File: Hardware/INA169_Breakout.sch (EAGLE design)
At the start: 21 parts, among them U1 INA169

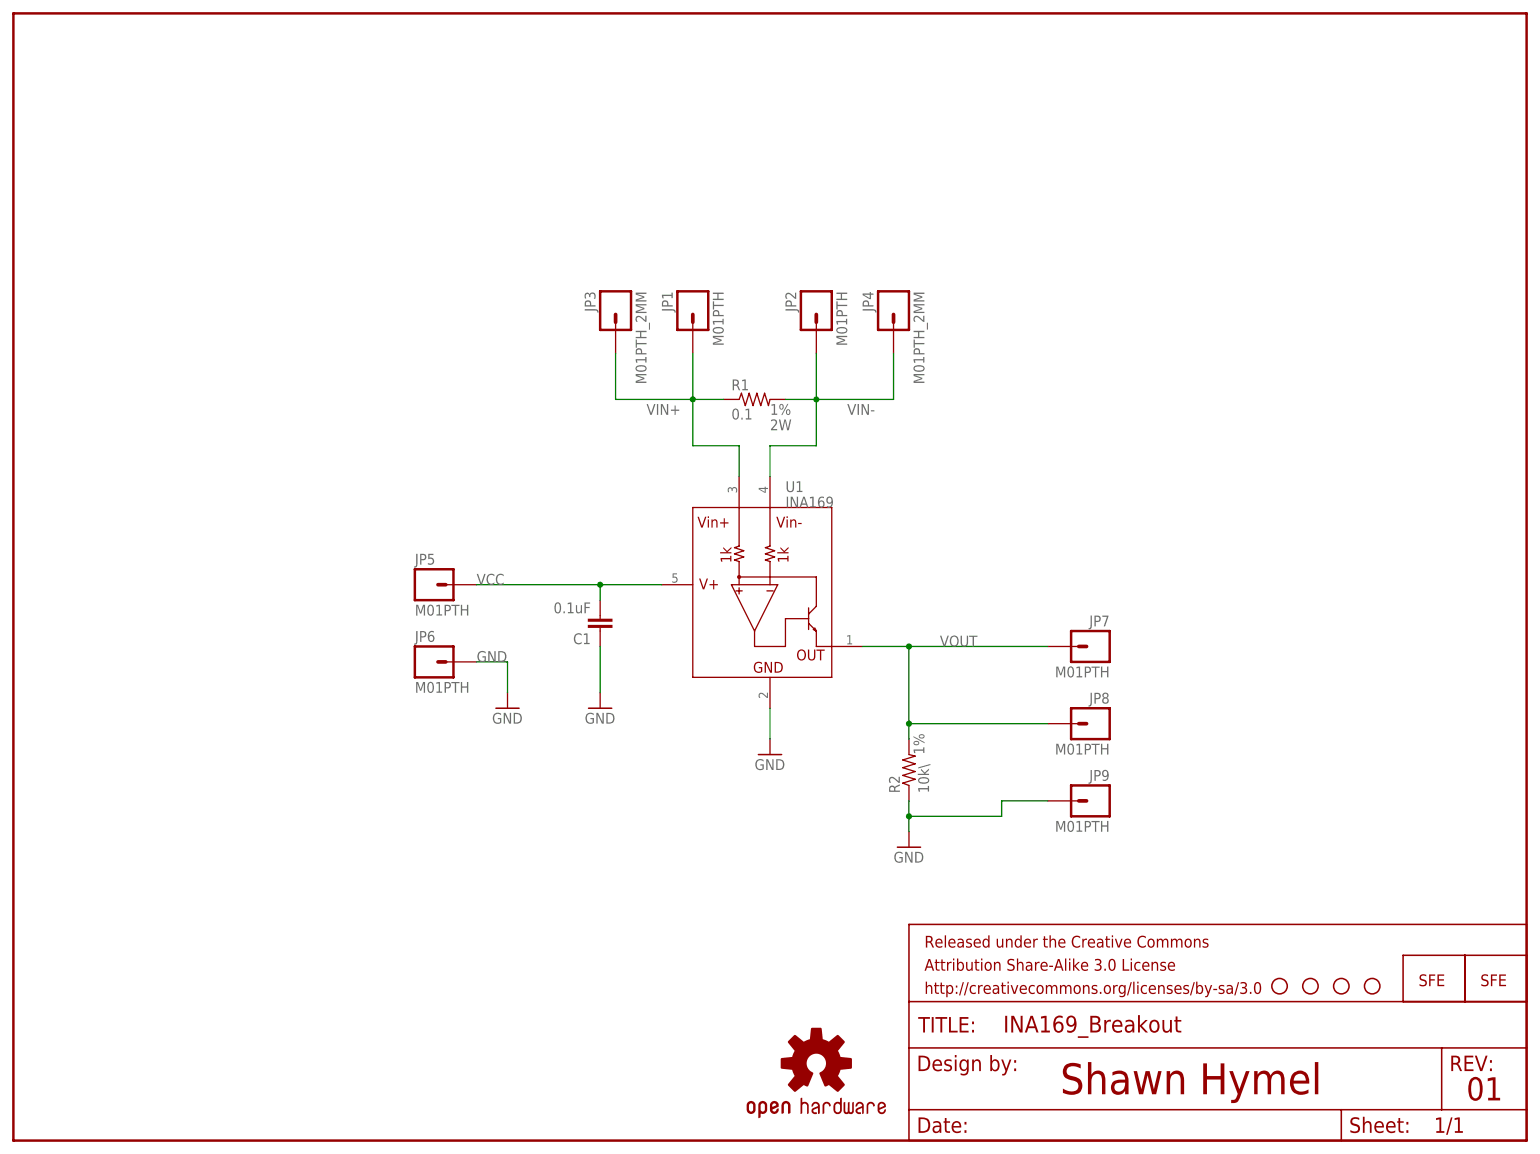
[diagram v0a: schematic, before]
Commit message: Fixed changes from board review. Ready for prototype.
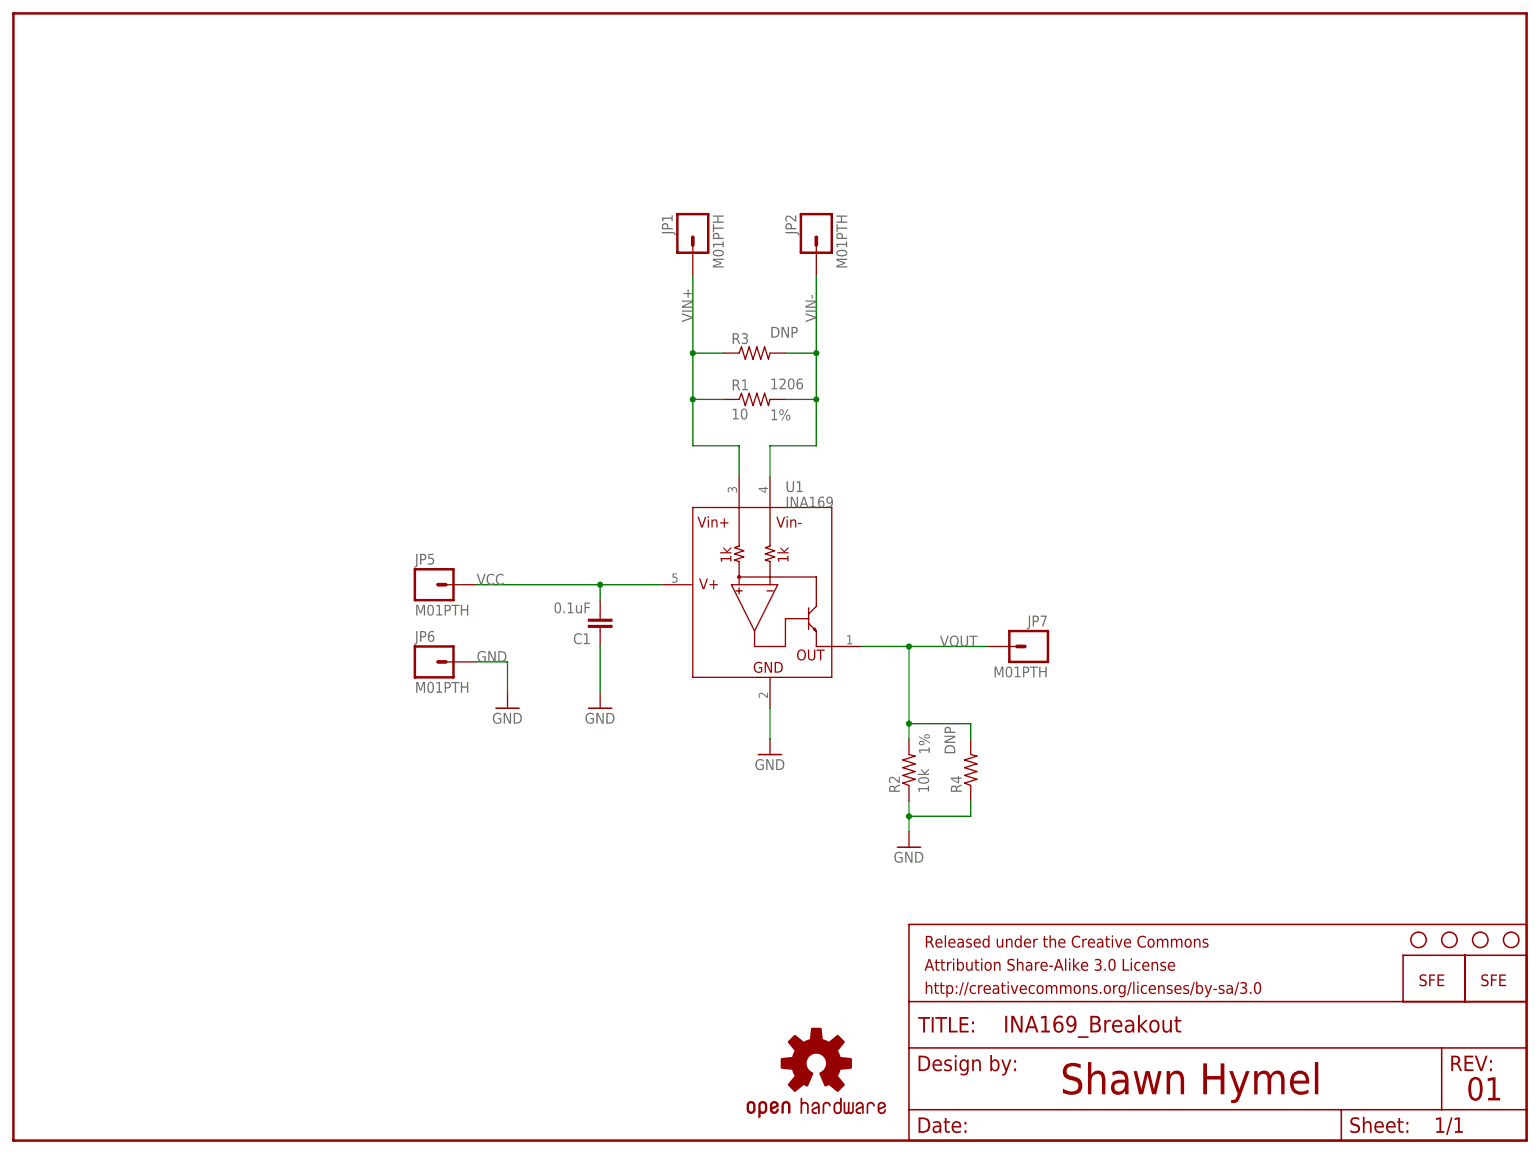
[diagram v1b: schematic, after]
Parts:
- removed JP3, JP4: M01PTH_2MM, SparkFun-Connectors:M01PTH_2MM
- removed JP8, JP9: M01PTH, SparkFun-Connectors:M01PTH
- added R3: (no value), SparkFun-Resistors:RESISTORPTH-2W
- added R4: (no value), SparkFun-Resistors:RESISTORPTH-1/4W
- R1: value 0.1 -> 10; device SparkFun-Passives:RESISTOR2512 -> SparkFun-Resistors:RESISTOR1206; POW 2W -> (none); SIZE (none) -> 1206
- R2: value 10k\ -> 10k; device SparkFun-Passives:RESISTOR0603-RES -> SparkFun-Resistors:RESISTOR0603
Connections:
- net GND: now also R4.1; no longer JP9.1
- net VIN+: now also R3.1; no longer JP3.1
- net VIN-: now also R3.2; no longer JP4.1
- net VOUT: now also R4.2; no longer JP8.1
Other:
- moved on the sheet: JP1, JP2, JP7
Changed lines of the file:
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@@
 <drawing>
 <settings>
-<setting alwaysvectorfont="no"/>
+<setting alwaysvectorfont="yes"/>
 <setting verticaltext="up"/>
 </settings>
@@
 <part name="FRAME1" library="SparkFun-Aesthetics" deviceset="FRAME-LETTER" device=""/>
 <part name="U1" library="SparkFun-AnalogIC" deviceset="INA169" device=""/>
-<part name="R1" library="SparkFun-Passives" deviceset="RESISTOR" device="2512" value="0.1">
-<attribute name="POW" value="2W"/>
-<attribute name="TOL" value="1%"/>
-</part>
 <part name="JP1" library="SparkFun-Connectors" deviceset="M01" device="PTH"/>
 <part name="JP2" library="SparkFun-Connectors" deviceset="M01" device="PTH"/>
-<part name="JP3" library="SparkFun-Connectors" deviceset="M01" device="PTH_2MM"/>
-<part name="JP4" library="SparkFun-Connectors" deviceset="M01" device="PTH_2MM"/>
 <part name="JP5" library="SparkFun-Connectors" deviceset="M01" device="PTH"/>
 <part name="JP6" library="SparkFun-Connectors" deviceset="M01" device="PTH"/>
 <part name="JP7" library="SparkFun-Connectors" deviceset="M01" device="PTH"/>
-<part name="R2" library="SparkFun-Passives" deviceset="RESISTOR" device="0603-RES" value="10k\">
-<attribute name="TOL" value="1%"/>
-</part>
 <part name="C1" library="SparkFun-Passives" deviceset="CAP" device="0603-CAP" value="0.1uF"/>
 <part name="STANDOFF1" library="SparkFun-Electromechanical" deviceset="STAND-OFF" device=""/>
@@
 <part name="GND3" library="SparkFun-Aesthetics" deviceset="GND" device=""/>
 <part name="GND4" library="SparkFun-Aesthetics" deviceset="GND" device=""/>
-<part name="JP8" library="SparkFun-Connectors" deviceset="M01" device="PTH"/>
-<part name="JP9" library="SparkFun-Connectors" deviceset="M01" device="PTH"/>
+<part name="R3" library="SparkFun-Resistors" deviceset="RESISTOR" device="PTH-2W">
+<attribute name="PLACE" value="DNP"/>
+</part>
+<part name="R4" library="SparkFun-Resistors" deviceset="RESISTOR" device="PTH-1/4W">
+<attribute name="PLACE" value="DNP"/>
+</part>
+<part name="R2" library="SparkFun-Resistors" deviceset="RESISTOR" device="0603" value="10k">
+<attribute name="TOL" value="1%"/>
+</part>
+<part name="R1" library="SparkFun-Resistors" deviceset="RESISTOR" device="1206" value="10">
+<attribute name="SIZE" value="1206"/>
+<attribute name="TOL" value="1%"/>
+</part>
 </parts>
 <sheets>
@@
 <instance part="FRAME1" gate="G$2" x="147.32" y="0"/>
 <instance part="U1" gate="G$1" x="124.46" y="88.9"/>
-<instance part="R1" gate="G$1" x="121.92" y="121.92">
-<attribute name="TOL" x="124.46" y="119.38" size="1.778" layer="96"/>
-<attribute name="POW" x="124.46" y="116.84" size="1.778" layer="96"/>
-</instance>
-<instance part="JP1" gate="G$1" x="111.76" y="137.16" rot="MR270"/>
-<instance part="JP2" gate="G$1" x="132.08" y="137.16" rot="MR270"/>
-<instance part="JP3" gate="G$1" x="99.06" y="137.16" rot="MR270"/>
-<instance part="JP4" gate="G$1" x="144.78" y="137.16" rot="MR270"/>
+<instance part="JP1" gate="G$1" x="111.76" y="149.86" rot="MR270"/>
+<instance part="JP2" gate="G$1" x="132.08" y="149.86" rot="MR270"/>
 <instance part="JP5" gate="G$1" x="68.58" y="91.44"/>
 <instance part="JP6" gate="G$1" x="68.58" y="78.74"/>
-<instance part="JP7" gate="G$1" x="177.8" y="81.28" rot="MR0"/>
-<instance part="R2" gate="G$1" x="147.32" y="60.96" rot="R90">
-<attribute name="TOL" x="149.86" y="63.5" size="1.778" layer="96" rot="R90"/>
-</instance>
+<instance part="JP7" gate="G$1" x="167.64" y="81.28" rot="MR0"/>
 <instance part="C1" gate="G$1" x="96.52" y="86.36" rot="R180"/>
-<instance part="STANDOFF1" gate="G$1" x="223.52" y="25.4"/>
-<instance part="STANDOFF2" gate="G$1" x="218.44" y="25.4"/>
-<instance part="STANDOFF3" gate="G$1" x="213.36" y="25.4"/>
-<instance part="STANDOFF4" gate="G$1" x="208.28" y="25.4"/>
+<instance part="STANDOFF1" gate="G$1" x="246.38" y="33.02"/>
+<instance part="STANDOFF2" gate="G$1" x="241.3" y="33.02"/>
+<instance part="STANDOFF3" gate="G$1" x="236.22" y="33.02"/>
+<instance part="STANDOFF4" gate="G$1" x="231.14" y="33.02"/>
 <instance part="LOGO1" gate="G$1" x="241.3" y="25.4"/>
 <instance part="LOGO2" gate="G$1" x="132.08" y="12.7"/>
@@
 <instance part="GND3" gate="1" x="124.46" y="63.5"/>
 <instance part="GND4" gate="1" x="147.32" y="48.26"/>
-<instance part="JP8" gate="G$1" x="177.8" y="68.58" rot="MR0"/>
-<instance part="JP9" gate="G$1" x="177.8" y="55.88" rot="MR0"/>
+<instance part="R3" gate="G$1" x="121.92" y="129.54" smashed="yes">
+<attribute name="PLACE" x="124.46" y="132.08" size="1.778" layer="96"/>
+<attribute name="NAME" x="118.11" y="131.0386" size="1.778" layer="95"/>
+<attribute name="VALUE" x="118.11" y="126.238" size="1.778" layer="96"/>
+</instance>
+<instance part="R4" gate="G$1" x="157.48" y="60.96" rot="R90">
+<attribute name="PLACE" x="154.94" y="63.5" size="1.778" layer="96" rot="R90"/>
+</instance>
+<instance part="R2" gate="G$1" x="147.32" y="60.96" rot="R90">
+<attribute name="TOL" x="149.86" y="63.5" size="1.778" layer="96" rot="R90" align="center-left"/>
+</instance>
+<instance part="R1" gate="G$1" x="121.92" y="121.92">
+<attribute name="SIZE" x="124.46" y="124.46" size="1.778" layer="96" align="center-left"/>
+<attribute name="TOL" x="124.46" y="119.38" size="1.778" layer="96" align="center-left"/>
+</instance>
 </instances>
 <busses>
@@
 <net name="VIN+" class="0">
 <segment>
-<pinref part="JP3" gate="G$1" pin="1"/>
-<wire x1="99.06" y1="129.54" x2="99.06" y2="121.92" width="0.1524" layer="91"/>
-<pinref part="R1" gate="G$1" pin="1"/>
-<wire x1="99.06" y1="121.92" x2="111.76" y2="121.92" width="0.1524" layer="91"/>
 <pinref part="JP1" gate="G$1" pin="1"/>
 <wire x1="111.76" y1="121.92" x2="116.84" y2="121.92" width="0.1524" layer="91"/>
+<wire x1="111.76" y1="142.24" x2="111.76" y2="129.54" width="0.1524" layer="91"/>
 <wire x1="111.76" y1="129.54" x2="111.76" y2="121.92" width="0.1524" layer="91"/>
 <wire x1="111.76" y1="121.92" x2="111.76" y2="114.3" width="0.1524" layer="91"/>
@@
 <wire x1="119.38" y1="114.3" x2="119.38" y2="109.22" width="0.1524" layer="91"/>
 <junction x="111.76" y="121.92"/>
-<label x="104.14" y="119.38" size="1.778" layer="95"/>
+<pinref part="R3" gate="G$1" pin="1"/>
+<wire x1="116.84" y1="129.54" x2="111.76" y2="129.54" width="0.1524" layer="91"/>
+<junction x="111.76" y="129.54"/>
+<label x="111.76" y="134.62" size="1.778" layer="95" rot="R90"/>
+<pinref part="R1" gate="G$1" pin="1"/>
 </segment>
 </net>
 <net name="VIN-" class="0">
 <segment>
-<pinref part="R1" gate="G$1" pin="2"/>
 <pinref part="JP2" gate="G$1" pin="1"/>
 <wire x1="127" y1="121.92" x2="132.08" y2="121.92" width="0.1524" layer="91"/>
 <wire x1="132.08" y1="121.92" x2="132.08" y2="129.54" width="0.1524" layer="91"/>
-<pinref part="JP4" gate="G$1" pin="1"/>
-<wire x1="132.08" y1="121.92" x2="144.78" y2="121.92" width="0.1524" layer="91"/>
-<wire x1="144.78" y1="121.92" x2="144.78" y2="129.54" width="0.1524" layer="91"/>
+<wire x1="132.08" y1="129.54" x2="132.08" y2="142.24" width="0.1524" layer="91"/>
 <wire x1="132.08" y1="121.92" x2="132.08" y2="114.3" width="0.1524" layer="91"/>
 <wire x1="132.08" y1="114.3" x2="124.46" y2="114.3" width="0.1524" layer="91"/>
@@
 <wire x1="124.46" y1="114.3" x2="124.46" y2="109.22" width="0.1524" layer="91"/>
 <junction x="132.08" y="121.92"/>
-<label x="137.16" y="119.38" size="1.778" layer="95"/>
+<pinref part="R3" gate="G$1" pin="2"/>
+<wire x1="127" y1="129.54" x2="132.08" y2="129.54" width="0.1524" layer="91"/>
+<junction x="132.08" y="129.54"/>
+<label x="132.08" y="134.62" size="1.778" layer="95" rot="R90"/>
+<pinref part="R1" gate="G$1" pin="2"/>
 </segment>
 </net>
@@
 <pinref part="JP7" gate="G$1" pin="1"/>
 <wire x1="139.7" y1="81.28" x2="147.32" y2="81.28" width="0.1524" layer="91"/>
-<wire x1="147.32" y1="81.28" x2="170.18" y2="81.28" width="0.1524" layer="91"/>
+<wire x1="147.32" y1="81.28" x2="160.02" y2="81.28" width="0.1524" layer="91"/>
 <wire x1="147.32" y1="66.04" x2="147.32" y2="68.58" width="0.1524" layer="91"/>
 <junction x="147.32" y="81.28"/>
 <label x="152.4" y="81.28" size="1.778" layer="95"/>
+<wire x1="147.32" y1="68.58" x2="147.32" y2="81.28" width="0.1524" layer="91"/>
+<junction x="147.32" y="68.58"/>
+<pinref part="R4" gate="G$1" pin="2"/>
+<wire x1="157.48" y1="68.58" x2="147.32" y2="68.58" width="0.1524" layer="91"/>
+<wire x1="157.48" y1="66.04" x2="157.48" y2="68.58" width="0.1524" layer="91"/>
 <pinref part="R2" gate="G$1" pin="2"/>
-<pinref part="JP8" gate="G$1" pin="1"/>
-<wire x1="147.32" y1="68.58" x2="147.32" y2="81.28" width="0.1524" layer="91"/>
-<wire x1="170.18" y1="68.58" x2="147.32" y2="68.58" width="0.1524" layer="91"/>
-<junction x="147.32" y="68.58"/>
 </segment>
 </net>
@@
 <segment>
 <wire x1="147.32" y1="55.88" x2="147.32" y2="53.34" width="0.1524" layer="91"/>
+<pinref part="GND4" gate="1" pin="GND"/>
+<wire x1="147.32" y1="53.34" x2="147.32" y2="50.8" width="0.1524" layer="91"/>
+<junction x="147.32" y="53.34"/>
+<pinref part="R4" gate="G$1" pin="1"/>
+<wire x1="157.48" y1="53.34" x2="147.32" y2="53.34" width="0.1524" layer="91"/>
+<wire x1="157.48" y1="55.88" x2="157.48" y2="53.34" width="0.1524" layer="91"/>
 <pinref part="R2" gate="G$1" pin="1"/>
-<pinref part="GND4" gate="1" pin="GND"/>
-<pinref part="JP9" gate="G$1" pin="1"/>
-<wire x1="147.32" y1="53.34" x2="147.32" y2="50.8" width="0.1524" layer="91"/>
-<wire x1="170.18" y1="55.88" x2="162.56" y2="55.88" width="0.1524" layer="91"/>
-<wire x1="162.56" y1="55.88" x2="162.56" y2="53.34" width="0.1524" layer="91"/>
-<wire x1="162.56" y1="53.34" x2="147.32" y2="53.34" width="0.1524" layer="91"/>
-<junction x="147.32" y="53.34"/>
-</segment>
-</net>
+</segment>
+</net>
